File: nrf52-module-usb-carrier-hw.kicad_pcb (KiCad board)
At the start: 2 copper layers, 38.1 x 50.8 mm, 63 parts, among them J1 USB_C_Receptacle_USB2.0_16P, J2 Conn_ARM_JTAG_SWD_10, SW1 SW_Push, SW2 SW_Push, U1 XC6206PxxxMR, U2 USBLC6-2SC6, U3 CH340N, U4 E73-2G4M04S1B, U5 LSM6DSO, U6 W25Q128JVS, U7 LIS3MDL, U8 PCA9557PW

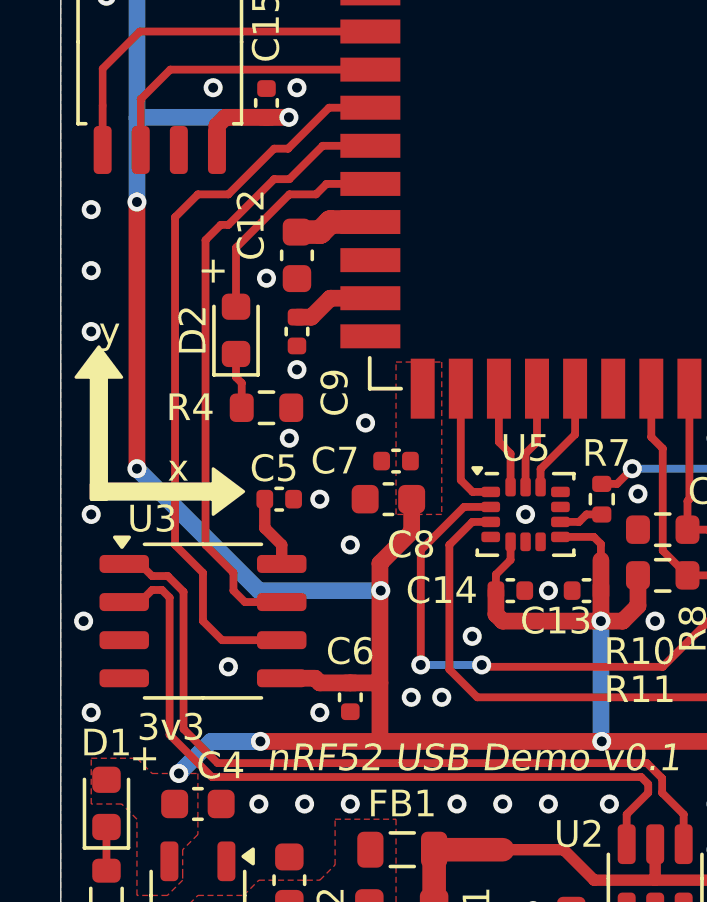
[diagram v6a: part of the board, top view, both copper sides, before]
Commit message: Switched around debug LED pinout with a UART line to be compatible with a previous design
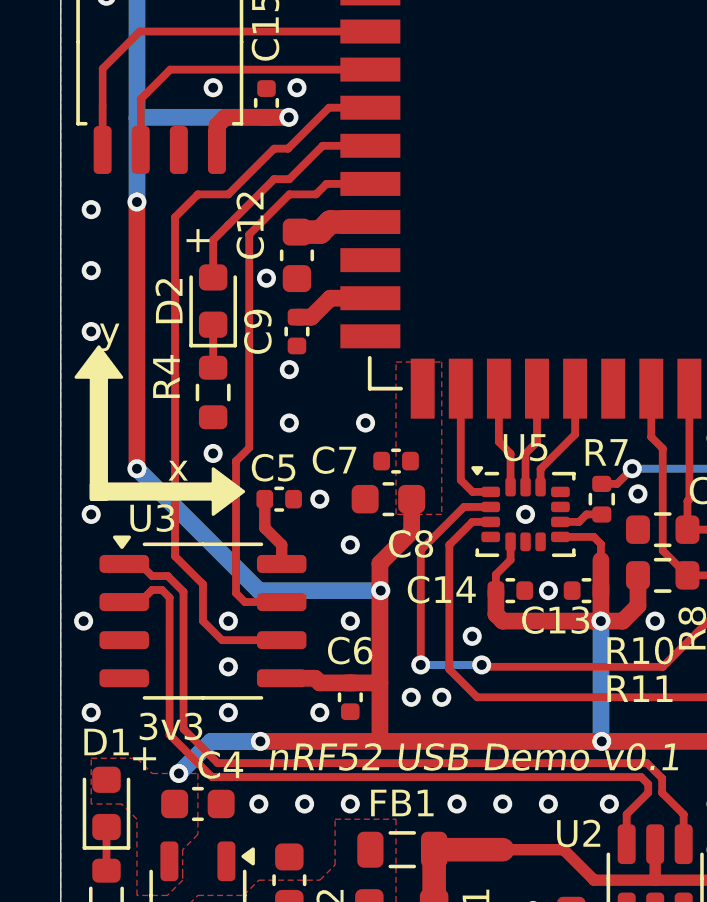
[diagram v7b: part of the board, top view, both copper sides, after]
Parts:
- moved R4 1.85 mm to (94.5, 82.3), turned to 90 degrees
- moved D2 1.24 mm to (94.5, 79.2)
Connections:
- U4 pad 10: /Power + MCU + SWD/UART_TX -> /Power + MCU + SWD/DEBUG_LED_A
- U4 pad 11: /Power + MCU + SWD/DEBUG_LED_A -> /Power + MCU + SWD/UART_TX
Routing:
- net /Power + MCU + SWD/UART_TX: track 20.6 -> 18.5 mm
- net /Power + MCU + SWD/DEBUG_LED_C: track 2.01 -> 1.44 mm
- net GND: vias 70 -> 74

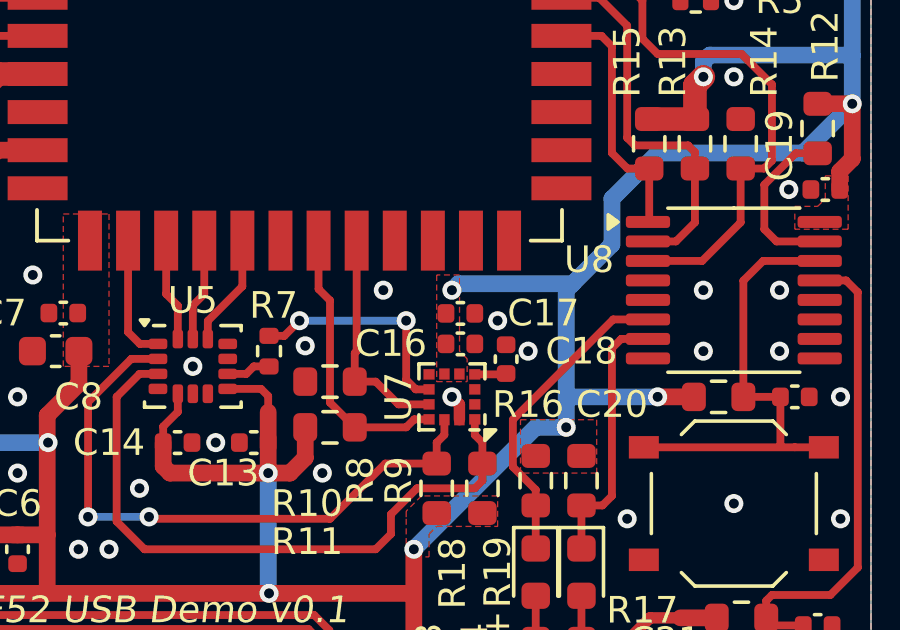
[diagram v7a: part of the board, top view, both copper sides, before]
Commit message: Brought out INT pin from magnetometer to MCU, in case of need.  Updated layout accordingly
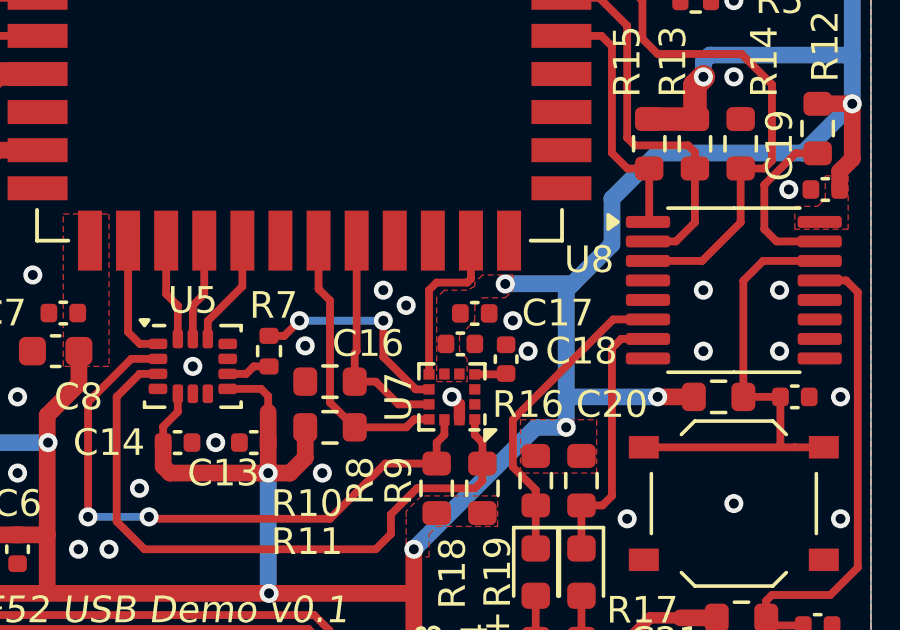
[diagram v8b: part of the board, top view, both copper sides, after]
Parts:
- moved C17 0.48 mm to (114.3, 84.6)
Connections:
- U4 pad 26: unconnected-(U4-P0.11-Pad26) -> MAG_INT
- U7 pad 7: /Peripherals/MAG_INT -> MAG_INT
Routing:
- net MAG_INT: track 0.00 -> 5.63 mm
- net +3V3: track 166.6 -> 164.8 mm
- net GND: vias 74 -> 75
